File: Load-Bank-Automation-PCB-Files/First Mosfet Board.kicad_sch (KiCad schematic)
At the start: 5 parts, among them J24 PHNX_CONN_1017521, U9 MCP6007

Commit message: Revision before Hall Effect Sensor
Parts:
- added C39, C40: 100u, symbol Device:C
- added C41: C, symbol Device:C
- added D8: D, symbol Device:D
- added D9: LED, symbol Device:LED
- added R32, R34: 10k, symbol Device:R
- added R33: 10m, symbol Device:R
- added R35: 186k25, symbol Device:R
- added R36: 13k75, symbol Device:R
- added R37, R38: 400k, symbol Device:R
- added R39, R41: R, symbol Device:R
- added U11: MCP6007, Package_SO:SOIC-8_3.9x4.9mm_P1.27mm, symbol EcoCar_Library:MCP6007
- U10: value ~ -> IRS10752LPBF; footprint (none) -> Package_TO_SOT_SMD:SOT-23-6
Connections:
- net GNDREF is gone; now on net V_{OUT}: J24.2
- net +12V: now also C39.2, D8.2 (A)
- net GND: now also C39.1, D9.1 (K), R36.2, R38.2
- net Current_ADC: now reaches U9.1
- net Current_ADC: now also R37.1
- net at U9.2 (-): now also R34.2, R37.2
- net at U10.4 (V_{B}): now also C40.2, D8.1 (K)
- net at U10.6 (V_{s}): now also C40.1
- net V_{OUT}: now reaches Q3.1 (S), Q3.2 (S), Q3.3 (S)
- net V_{OUT}: now also R39.1, R41.1
- new net: C41.1, Q3.5 (D), R33.1, R34.1, R35.2
- new net: C41.2, R41.2
- new net: R35.1, R36.1, U11.3 (+)
- new net: R32.2, R38.1, U9.3 (+)
- new net: D9.2 (A), R39.2
- new net V_{IN}: J24.1, R32.1, R33.2
- new net Voltage_ADC: U11.1, U11.2 (-)
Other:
- note added: "- See if you should use an op amp or hall effect sensor for current sensing (use opamp) - How many IDC pins do I need (Talked to Abi and the IDCs come only in even numbers, not odd) - Add LEDs - Double check power desipated by gate driver (Talked with abi and no need to do so) - Calculate bootstrap capacitor - Calculte HO pin resistor value - Use a voltage divider to measure voltage (Voltage shou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"
- note added: "48V * R36/(R35+R36) = 3V3"
- note added: "Boostrap Gate Driver"
- note added: "Creat a snubber circuit for Transient responses"
- note added: "Current Opamp"
- note added: "Current_ADC = V_{R33}*(R38/R32) ||| R38=R37 & R32=R34"
- note added: "MOSFET Board #1"
- note added: "Make sure that the mosfet can handle 10A"
- note added: "Pick a Diode that can handle at least 72V"
- note added: "Terminal Block"
- note added: "Voltage Opamp"
- note removed: "- See if you should use an op amp or hall effect sensor for current sensing - How many IDC pins do I need (Talked to Abi and the IDCs come only in even numbers, not odd) - Add LEDs - Double check power desipated by gate driver (Talked with abi and no need to do so) - Calculate bootstrap capacitor - Calculte HO pin resistor value - Use a voltage divider to measure voltage (coltage should be less t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"
- moved on the sheet: J24, Q3, R30, U10, U9A

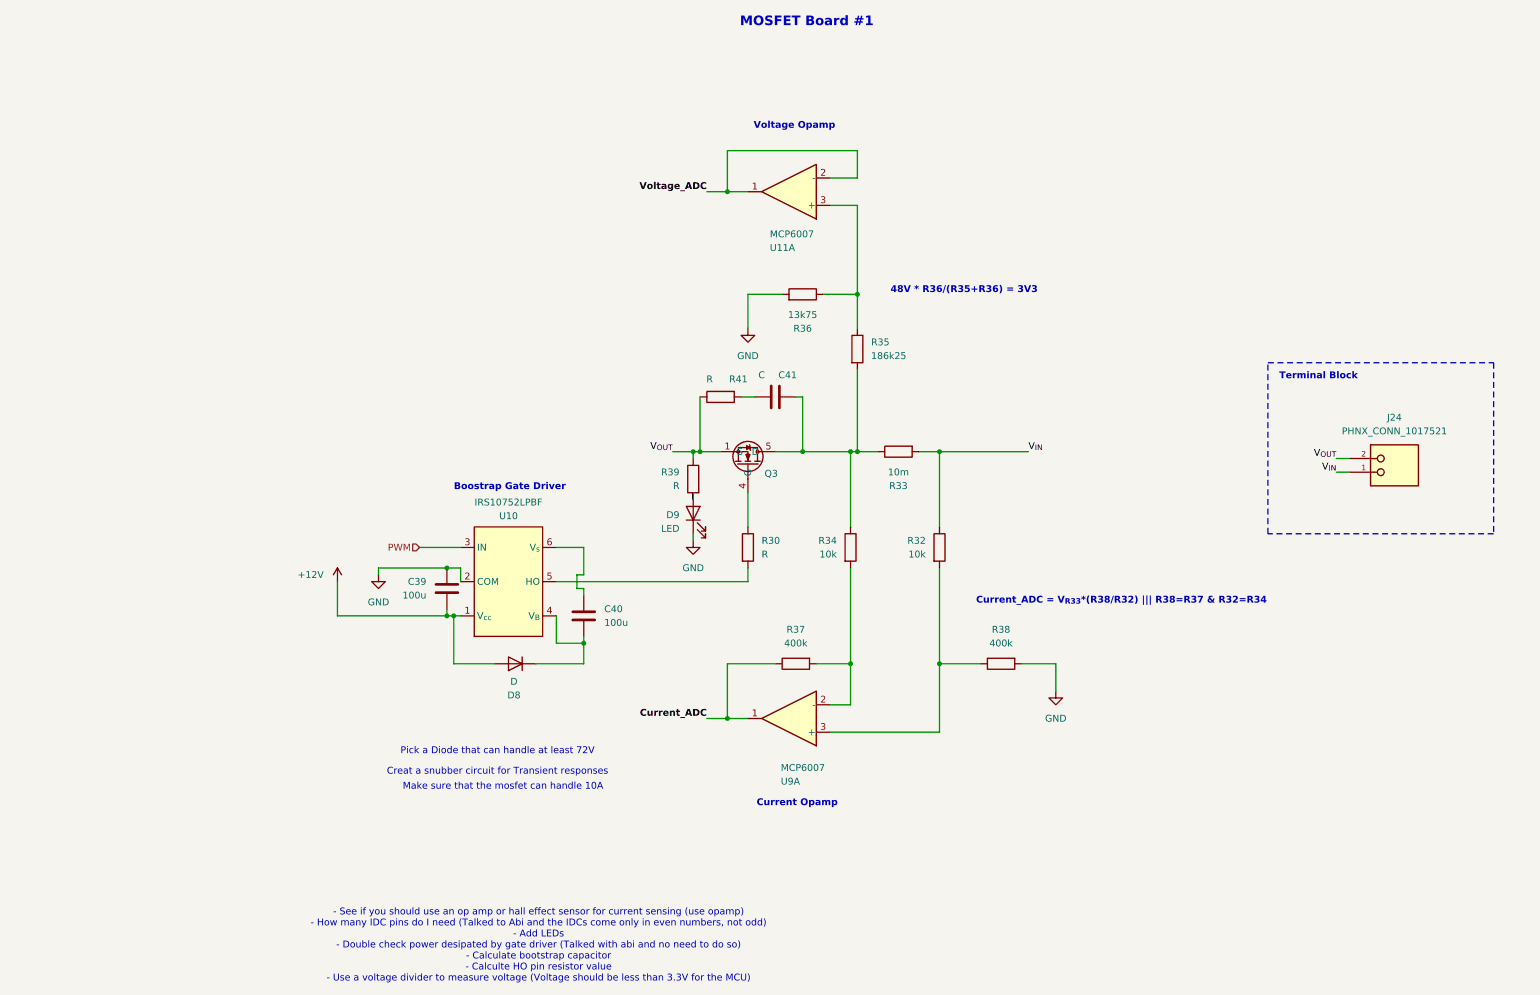
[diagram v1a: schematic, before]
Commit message: Comlpeted Schematic(needs some small component values only)
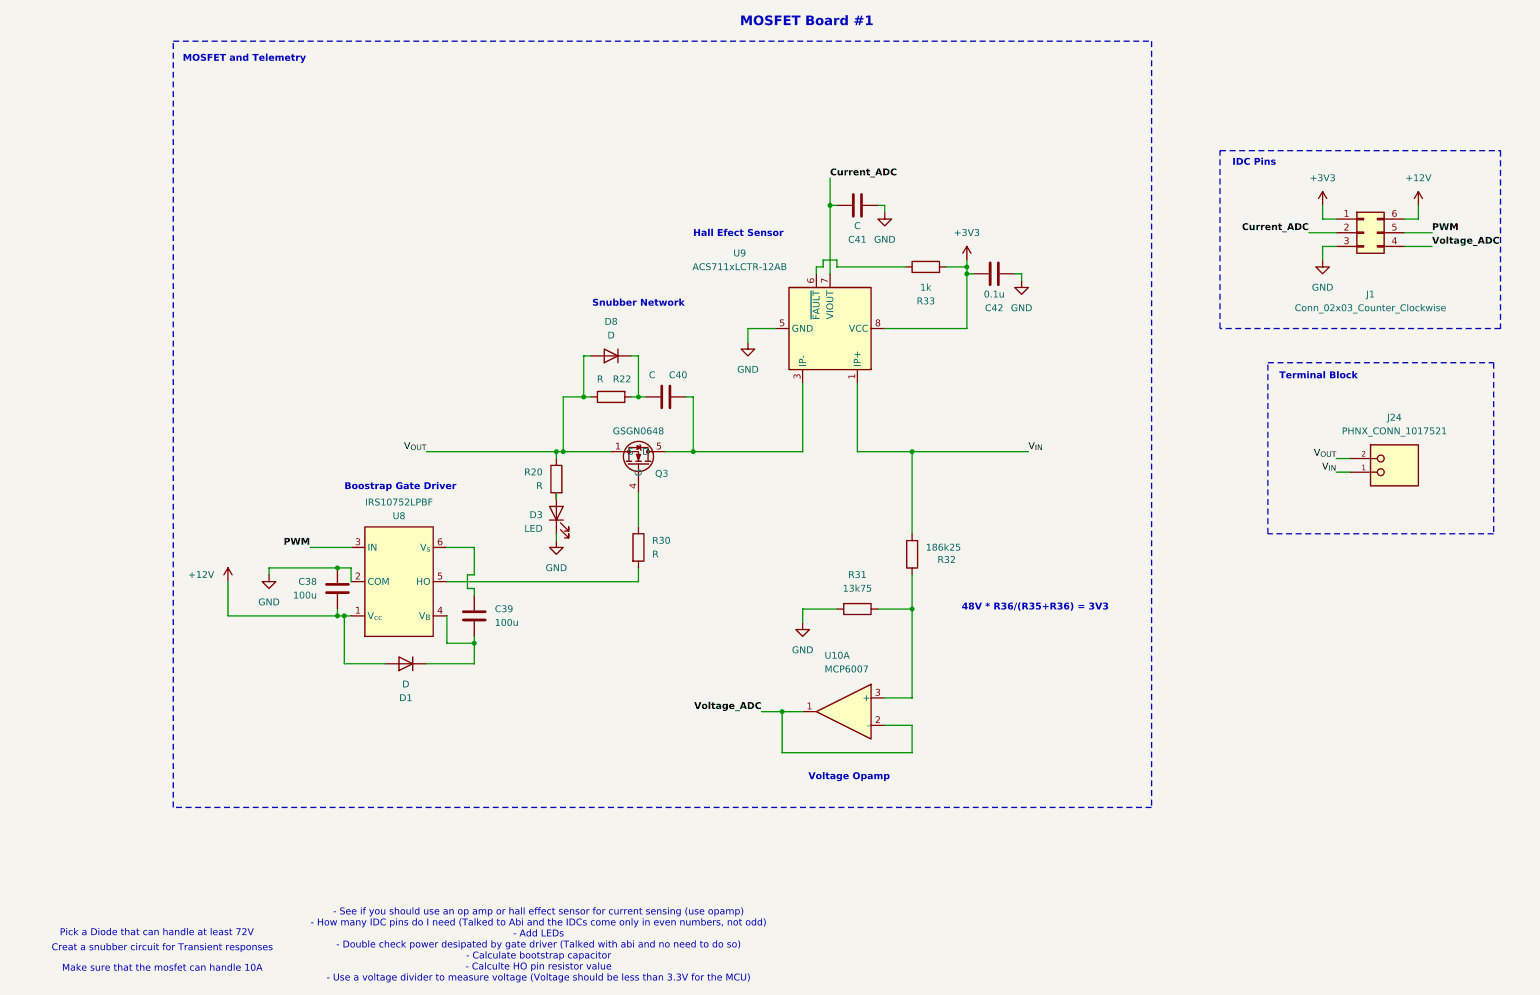
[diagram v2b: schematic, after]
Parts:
- removed R32, R34: 10k, symbol Device:R
- removed R37, R38: 400k, symbol Device:R
- removed U9: MCP6007, Package_SO:SOIC-8_3.9x4.9mm_P1.27mm, symbol EcoCar_Library:MCP6007
- added C41: C, symbol Device:C
- added C42: 0.1u, symbol Device:C
- added D1: D, symbol Device:D
- added J1: Conn_02x03_Counter_Clockwise, Connector_IDC:IDC-Header_2x03_P2.54mm_Vertical, symbol Connector_Generic:Conn_02x03_Counter_Clockwise
- added U9: ACS711xLCTR-12AB, Package_SO:SOIC-8_3.9x4.9mm_P1.27mm, symbol Sensor_Current:ACS711xLCTR-12AB
- Q3: value ~ -> GSGN0648; footprint (none) -> Package_TO_SOT_SMD:Goodarksemiconductor_PPAK_3x3
- R33: value 10m -> 1k
- renumbered C39 to C38, C40 to C39, C41 to C40, D9 to D3, R39 to R20, R41 to R22, R36 to R31, R35 to R32, U11 to U10, U10 to U8
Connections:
- net +12V: now also D1.2 (A), J1.6 (Pin_6); no longer D8.2 (A)
- net Current_ADC: now also C41.2, J1.2 (Pin_2), U9.7 (VIOUT)
- net GND: now also C41.1, C42.1, J1.3 (Pin_3), U9.5 (GND)
- net PWM: now also J1.5 (Pin_5)
- net V_{IN}: now also R32.2, U9.1 (IP+), U9.2 (IP+); no longer R33.2
- net V_{OUT}: now also D8.2 (A)
- net Voltage_ADC: now also J1.4 (Pin_4)
- net at C40.1, Q3.5 (D): now also U9.3 (IP-), U9.4 (IP-); no longer R32.2, R33.1
- net at C39.2, U8.4 (V_{B}): now also D1.1 (K); no longer D8.1 (K)
- net at C40.2, R22.2: now also D8.1 (K)
- new net: R33.1, U9.6 (~{FAULT})
- new net +3V3: C42.2, J1.1 (Pin_1), R33.2, U9.8 (VCC)
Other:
- note added: "Hall Efect Sensor"
- note added: "IDC Pins"
- note added: "MOSFET and Telemetry"
- note added: "Snubber Network"
- note removed: "Current Opamp"
- note removed: "Current_ADC = V_{R33}*(R38/R32) ||| R38=R37 & R32=R34"
- moved on the sheet: C38, C39, C40, D3, Q3, R20, R22, R30, R31, R32, U10A, U8

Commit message: Schematic revision for review
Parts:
- removed D8: D, symbol Device:D
- removed U10: MCP6007, Package_SO:SOIC-8_3.9x4.9mm_P1.27mm, symbol EcoCar_Library:MCP6007
- removed U9: ACS711xLCTR-12AB, Package_SO:SOIC-8_3.9x4.9mm_P1.27mm, symbol Sensor_Current:ACS711xLCTR-12AB
- added U10: MCP6006-OTVAO, Package_TO_SOT_SMD:SOT-23-5, symbol Amplifier_Operational:MCP6001-OT
- added U48: ACS711xLCTR-25AB, Package_SO:SOIC-8_3.9x4.9mm_P1.27mm, symbol Sensor_Current:ACS711xLCTR-25AB
- C38, C39, C40, C41, C42: footprint (none) -> Capacitor_SMD:C_0603_1608Metric_Pad1.08x0.95mm_HandSolder
- D1: value D -> STPS5H100SFY; footprint (none) -> Package_TO_SOT_SMD:TO-277A
- D3: footprint (none) -> LED_SMD:LED_0603_1608Metric_Pad1.05x0.95mm_HandSolder
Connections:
- net +3V3: now also U10.5 (V+), U48.8 (VCC)
- net Current_ADC: now also U48.7 (VIOUT)
- net GND: now also U10.2 (V-), U48.5 (GND)
- net V_{IN}: now also U48.1 (IP+), U48.2 (IP+)
- net Voltage_ADC: now also U10.1, U10.4 (-)
- net at C40.1, Q3.5 (D): now also U48.3 (IP-), U48.4 (IP-)
- net at R31.1, R32.1: now also U10.3 (+)
- net at R33.1: now also U48.6 (~{FAULT})
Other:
- note added: "Find common resistor values later"

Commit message: Saving Progress
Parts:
- removed C41: C, Capacitor_SMD:C_0603_1608Metric_Pad1.08x0.95mm_HandSolder, symbol Device:C
- removed C42: 0.1u, Capacitor_SMD:C_0603_1608Metric_Pad1.08x0.95mm_HandSolder, symbol Device:C
- removed R33: 1k, symbol Device:R
- removed U48: ACS711xLCTR-25AB, Package_SO:SOIC-8_3.9x4.9mm_P1.27mm, symbol Sensor_Current:ACS711xLCTR-25AB
- added D47: SBR1U200P1, Diode_SMD:D_PowerDI-123, symbol Device:D
- C40: value C -> 1u; footprint Capacitor_SMD:C_0603_1608Metric_Pad1.08x0.95mm_HandSolder -> (none)
- D1: value STPS5H100SFY -> CDBA5200-HF; footprint Package_TO_SOT_SMD:TO-277A -> Diode_SMD:D_SMA
- R20: value R -> 20k
- R22: value R -> 100k
- R30: value R -> 400
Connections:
- net V_{IN}: now also Q3.5 (D), R22.2, D47.2 (A)
- net V_{OUT}: now also C40.1; no longer R22.1
- net at C40.2: now also R22.1, D47.1 (K); no longer R22.2
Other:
- note added: "- Not sure if I should use a film or cermaic or other type of capacitor - See if it's feasible to put a lower/no resistance (Check power and current) - See if I can use the same diode for the Snubber and Gate driver (The gate driver diode says it is very high switching speed but does give it)"
- note added: "Capacitor V >= 120 Capacitor I >= 0.5A Capacitor peak power >= 8W Low ESL & ESR"
- note added: "Diode Vbrk > 120V Diode I >= 0.5A Diode peak power >= 8W"
- note added: "Resistor rated for 15W peak [(48V + 12V) * 150 mA = 9W]"
- note removed: "- See if you should use an op amp or hall effect sensor for current sensing (use opamp) - How many IDC pins do I need (Talked to Abi and the IDCs come only in even numbers, not odd) - Add LEDs - Double check power desipated by gate driver (Talked with abi and no need to do so) - Calculate bootstrap capacitor - Calculte HO pin resistor value - Use a voltage divider to measure voltage (Voltage shou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"
- note removed: "Creat a snubber circuit for Transient responses"
- note removed: "Hall Efect Sensor"
- note removed: "Make sure that the mosfet can handle 10A"
- note removed: "Pick a Diode that can handle at least 72V"

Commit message: Saving Progress (Changed eFuse and comments)
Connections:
- net Current_ADC: no longer names the net of J1.2 (Pin_2)
- no-connect marks 0 -> 1
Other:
- note added: "- Not sure if I should use a film or cermaic or other type of capacitor - See if it's feasible to put a lower/no resistance (Check power and current) - See if I can use the same diode for the Snubber and Gate driver (The gate driver diode says it is very high switching speed but does give it) - Do I need to add a resistor from 12V to the gate driver to limit current (transients)? - Do I need to a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"
- note added: "Vf = 0.9V"
- note removed: "- Not sure if I should use a film or cermaic or other type of capacitor - See if it's feasible to put a lower/no resistance (Check power and current) - See if I can use the same diode for the Snubber and Gate driver (The gate driver diode says it is very high switching speed but does give it)"
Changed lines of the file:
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@@
+		)
+	)
+	(text "Vf = 0.9V\n"
+		(exclude_from_sim no)
+		(at 77.47 144.272 0)
+		(effects
+			(font
+				(size 1.27 1.27)
+			)
 		)
 	)
@@
 		)
 	)
-	(text "- Not sure if I should use a film or cermaic or other type of capacitor\n- See if it's feasible to put a lower/no resistance (Check power and current)\n- See if I can use the same diode for the Snubber and Gate driver (The gate driver diode\nsays it is very high switching speed but does give it)"
-		(exclude_from_sim no)
-		(at 129.794 177.8 0)
+	(text "- Not sure if I should use a film or cermaic or other type of capacitor\n- See if it's feasible to put a lower/no resistance (Check power and current)\n- See if I can use the same diode for the Snubber and Gate driver (The gate driver diode\nsays it is very high switching speed but does give it)\n- Do I need to add a resistor from 12V to the gate driver to limit current (transients)?\n- Do I need to add a capacitor at the opamp output (limiting ADC transients from MCU)?"
+		(exclude_from_sim no)
+		(at 223.774 173.482 0)
 		(effects
 			(font
@@
 		(color 0 0 0 0)
 	)
+	(no_connect
+		(at 250.19 54.61)
+	)
 	(wire
 		(pts
@@
 		(pts
 			(xy 105.41 95.25) (xy 107.95 95.25)
-		)
-		(stroke
-			(width 0)
-			(type default)
-		)
-	)
-	(wire
-		(pts
-			(xy 245.11 54.61) (xy 250.19 54.61)
 		)
 		(stroke
@@
 			)
 			(justify right bottom)
-		)
-	)
-	(label "Current_ADC"
-		(at 245.11 54.61 180)
-		(effects
-			(font
-				(size 1.27 1.27)
-				(thickness 0.254)
-				(bold yes)
-			)
-			(justify right bottom)

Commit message: Schematic for revision
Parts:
- D1: value CDBA5200-HF -> SBR1U200P1; footprint Diode_SMD:D_SMA -> Diode_SMD:D_PowerDI-123
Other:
- note added: "Vf = 0.75 V"
- note removed: "Vf = 0.9V"
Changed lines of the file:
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@@
 		)
 	)
-	(text "Vf = 0.9V\n"
+	(text "Vf = 0.75 V\n"
 		(exclude_from_sim no)
 		(at 77.47 144.272 0)
@@
 	(text "- Not sure if I should use a film or cermaic or other type of capacitor\n- See if it's feasible to put a lower/no resistance (Check power and current)\n- See if I can use the same diode for the Snubber and Gate driver (The gate driver diode\nsays it is very high switching speed but does give it)\n- Do I need to add a resistor from 12V to the gate driver to limit current (transients)?\n- Do I need to add a capacitor at the opamp output (limiting ADC transients from MCU)?"
 		(exclude_from_sim no)
-		(at 223.774 173.482 0)
-		(effects
-			(font
-				(size 1.27 1.27)
-			)
+		(at 179.324 173.228 0)
+		(effects
+			(font
+				(size 1.27 1.27)
+			)
+			(justify left)
 		)
 	)
@@
 	(symbol
 		(lib_id "Device:D")
-		(at 77.47 134.62 180)
+		(at 77.47 134.62 0)
+		(mirror y)
 		(unit 1)
 		(exclude_from_sim no)
@@
 			)
 		)
-		(property "Value" "CDBA5200-HF"
+		(property "Value" "SBR1U200P1"
 			(at 77.47 138.43 0)
 			(effects
@@
 			)
 		)
-		(property "Footprint" "Diode_SMD:D_SMA"
+		(property "Footprint" "Diode_SMD:D_PowerDI-123"
 			(at 77.47 134.62 0)
 			(effects
@@
 			)
 		)
-		(property "Datasheet" "https://mm.digikey.com/Volume0/opasdata/d220001/medias/docus/506/CDBA540-HF-CDBA5200-HF_RevC.pdf"
+		(property "Datasheet" "https://www.digikey.ca/en/products/detail/diodes-incorporated/SBR1U200P1-7/2414250"
 			(at 77.47 134.62 0)
 			(effects
